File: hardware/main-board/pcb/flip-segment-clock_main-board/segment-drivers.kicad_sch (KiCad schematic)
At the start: 0 parts

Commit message: Refining design of the segment drivers
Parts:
- added C15, C16, C17, C18, C19, C20, C21, C22, C23, C24, C25, C26, C27, C28, C7, C8: 100 nF, Capacitor_SMD:C_0402_1005Metric, symbol Device:C_Small
- added C5: 10 uF, Capacitor_SMD:C_1206_3216Metric, symbol Device:C_Small
- added C6: 560 uF, Capacitor_SMD:C_Elec_10x10.2, symbol Device:C_Polarized_Small
- added D1, D2, D3, D4: D_Schottky_Small, symbol Device:D_Schottky_Small
- added IC10, IC11, IC12, IC13, IC14, IC15, IC16, IC17, IC4, IC5, IC6, IC7, IC8, IC9: A3909GLNTR-T, SamacSys_Parts:SOP100P600X175-10N, symbol SamacSys_Parts:A3909GLNTR-T
- added J3: Digit 1, TerminalBlock:TerminalBlock_Xinya_XY308-2.54-14P_1x14_P2.54mm_Horizontal, symbol Connector:Screw_Terminal_01x14
- added J4: Digit 2, TerminalBlock:TerminalBlock_Xinya_XY308-2.54-14P_1x14_P2.54mm_Horizontal, symbol Connector:Screw_Terminal_01x14
- added J5: Digit 3, TerminalBlock:TerminalBlock_Xinya_XY308-2.54-14P_1x14_P2.54mm_Horizontal, symbol Connector:Screw_Terminal_01x14
- added J6: Digit 4, TerminalBlock:TerminalBlock_Xinya_XY308-2.54-14P_1x14_P2.54mm_Horizontal, symbol Connector:Screw_Terminal_01x14
- added R5, R6: 100K, Resistor_SMD:R_0402_1005Metric, symbol Device:R_Small
- added TP3: SER, TestPoint:TestPoint_Pad_D1.5mm, symbol Connector:TestPoint
- added TP4: 12v, TestPoint:TestPoint_Pad_D1.5mm, symbol Connector:TestPoint
- added U1, U2: 74HC595, Package_SO:SOIC-16_3.9x9.9mm_P1.27mm, symbol 74xx:74HC595
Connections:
- new net: IC11.10 (OUT1), J5.1 (Pin_1)
- new net: IC11.6 (OUT4), J5.4 (Pin_4)
- new net: IC11.7 (OUT3), J5.3 (Pin_3)
- new net: IC11.9 (OUT2), J5.2 (Pin_2)
- new net: C25.2, D3.1 (K), D4.1 (K), IC14.3 (VBB)
- new net: IC16.10 (OUT1), J6.7 (Pin_7)
- new net: IC16.6 (OUT4), J6.10 (Pin_10)
- new net: IC16.7 (OUT3), J6.9 (Pin_9)
- new net: IC16.9 (OUT2), J6.8 (Pin_8)
- new net: IC4.10 (OUT1), J3.1 (Pin_1)
- new net: IC6.9 (OUT2), J3.10 (Pin_10)
- new net: IC6.7 (OUT3), J3.11 (Pin_11)
- new net: IC6.6 (OUT4), J3.12 (Pin_12)
- new net: IC7.10 (OUT1), J3.13 (Pin_13)
- new net: IC7.9 (OUT2), J3.14 (Pin_14)
- new net: IC4.9 (OUT2), J3.2 (Pin_2)
- new net: IC4.7 (OUT3), J3.3 (Pin_3)
- new net: IC4.6 (OUT4), J3.4 (Pin_4)
- new net: IC5.10 (OUT1), J3.5 (Pin_5)
- new net: IC5.9 (OUT2), J3.6 (Pin_6)
- new net: IC5.7 (OUT3), J3.7 (Pin_7)
- new net: IC5.6 (OUT4), J3.8 (Pin_8)
- new net: IC6.10 (OUT1), J3.9 (Pin_9)
- new net: IC13.9 (OUT2), J5.10 (Pin_10)
- new net: IC13.7 (OUT3), J5.11 (Pin_11)
- new net: IC13.6 (OUT4), J5.12 (Pin_12)
- new net: IC14.10 (OUT1), J5.13 (Pin_13)
- new net: IC14.9 (OUT2), J5.14 (Pin_14)
- new net: IC12.10 (OUT1), J5.5 (Pin_5)
- new net: IC12.9 (OUT2), J5.6 (Pin_6)
- new net: IC12.7 (OUT3), J5.7 (Pin_7)
- new net: IC12.6 (OUT4), J5.8 (Pin_8)
- new net: IC13.10 (OUT1), J5.9 (Pin_9)
- new net: U1.9 (QH'), U2.14 (SER)
- new net: C18.2, D1.1 (K), D2.1 (K), IC7.3 (VBB)
- new net: IC9.10 (OUT1), J4.7 (Pin_7)
- new net: IC9.6 (OUT4), J4.10 (Pin_10)
- new net: IC9.7 (OUT3), J4.9 (Pin_9)
- new net: IC9.9 (OUT2), J4.8 (Pin_8)
- new net: IC15.10 (OUT1), J6.3 (Pin_3)
- new net: IC15.6 (OUT4), J6.6 (Pin_6)
- new net: IC15.7 (OUT3), J6.5 (Pin_5)
- new net: IC15.9 (OUT2), J6.4 (Pin_4)
- new net: TP3.1, U1.14 (SER)
- new net: IC14.7 (OUT3), J6.1 (Pin_1)
- new net: IC17.10 (OUT1), J6.11 (Pin_11)
- new net: IC17.9 (OUT2), J6.12 (Pin_12)
- new net: IC17.7 (OUT3), J6.13 (Pin_13)
- new net: IC17.6 (OUT4), J6.14 (Pin_14)
- new net: IC14.6 (OUT4), J6.2 (Pin_2)
- new net: IC7.6 (OUT4), J4.2 (Pin_2)
- new net: IC7.7 (OUT3), J4.1 (Pin_1)
- new net: IC8.10 (OUT1), J4.3 (Pin_3)
- new net: IC8.6 (OUT4), J4.6 (Pin_6)
- new net: IC8.7 (OUT3), J4.5 (Pin_5)
- new net: IC8.9 (OUT2), J4.4 (Pin_4)
- new net: IC10.10 (OUT1), J4.11 (Pin_11)
- new net: IC10.9 (OUT2), J4.12 (Pin_12)
- new net: IC10.7 (OUT3), J4.13 (Pin_13)
- new net: IC10.6 (OUT4), J4.14 (Pin_14)
- new net +12V: C5.2, C6.1, TP4.1
- new net +3.3V: C7.2, C8.2, R5.1, R6.1, U1.16 (VCC), U2.16 (VCC)
- new net A1: U1.15 (QA)
- new net A2: U1.1 (QB)
- new net B3: U1.2 (QC)
- new net B4: U1.3 (QD)
- new net C1: U1.4 (QE)
- new net C2: U1.5 (QF)
- new net C3: U1.6 (QG)
- new net C4: U1.7 (QH)
- new net D1: U2.15 (QA)
- new net D2: U2.1 (QB)
- new net DIG1: C15.2, C16.2, C17.2, D1.2 (A), IC4.3 (VBB), IC5.3 (VBB), IC6.3 (VBB)
- new net DIG2: C19.2, C20.2, C21.2, D2.2 (A), IC10.3 (VBB), IC8.3 (VBB), IC9.3 (VBB)
- new net DIG3: C22.2, C23.2, C24.2, D4.2 (A), IC11.3 (VBB), IC12.3 (VBB), IC13.3 (VBB)
- new net DIG4: C26.2, C27.2, C28.2, D3.2 (A), IC15.3 (VBB), IC16.3 (VBB), IC17.3 (VBB)
- new net E3: U2.2 (QC)
- new net E4: U2.3 (QD)
- new net F1: U2.4 (QE)
- new net F2: U2.5 (QF)
- new net GND: C15.1, C16.1, C17.1, C18.1, C19.1, C20.1, C21.1, C22.1, C23.1, C24.1, C25.1, C26.1, C27.1, C28.1, C5.1, C6.2, C7.1, C8.1, IC10.8 (GND), IC11.8 (GND), IC12.8 (GND), IC13.8 (GND), IC14.8 (GND), IC15.8 (GND), IC16.8 (GND), IC17.8 (GND), IC4.8 (GND), IC5.8 (GND), IC6.8 (GND), IC7.8 (GND), IC8.8 (GND), IC9.8 (GND), U1.8 (GND), U2.8 (GND)
- new net NOE: U1.13 (~{OE}), U2.13 (~{OE})
- new net NSRCLR: R5.2, U1.10 (~{SRCLR}), U2.10 (~{SRCLR})
- new net RCLCK: U1.12 (RCLK), U2.12 (RCLK)
- new net SRCLK: R6.2, U1.11 (SRCLK), U2.11 (SRCLK)
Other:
- note added: "A3909 Cluster"
- note added: "Bypass and Bulk Decoupling"
- note added: "H-Bridge Drivers"
- note added: "One 100 nF cap per IC, one 10 uF and one 470 uF for bulk (prevent major voltage droop during pulses)"
- note added: "Placeholder explaination"

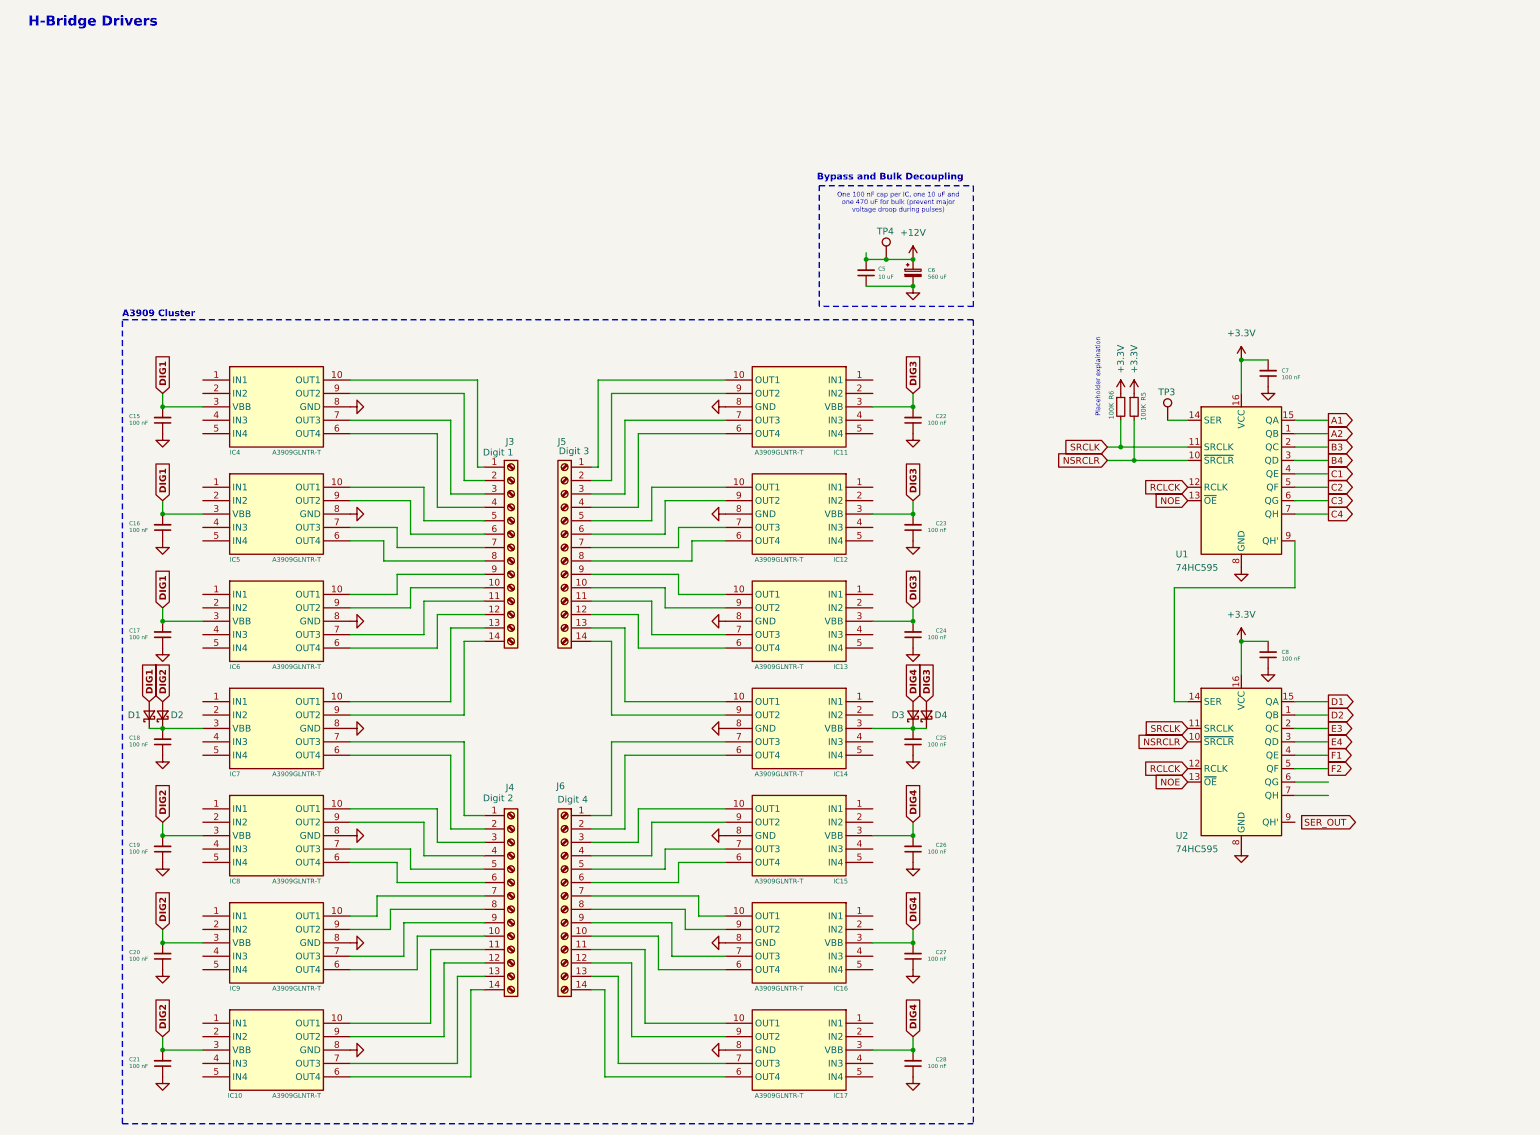
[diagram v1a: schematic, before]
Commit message: Segment driver update
Continuing refinement of segment driver design, settle on per digit vbb isolation, no overlapping between a3909
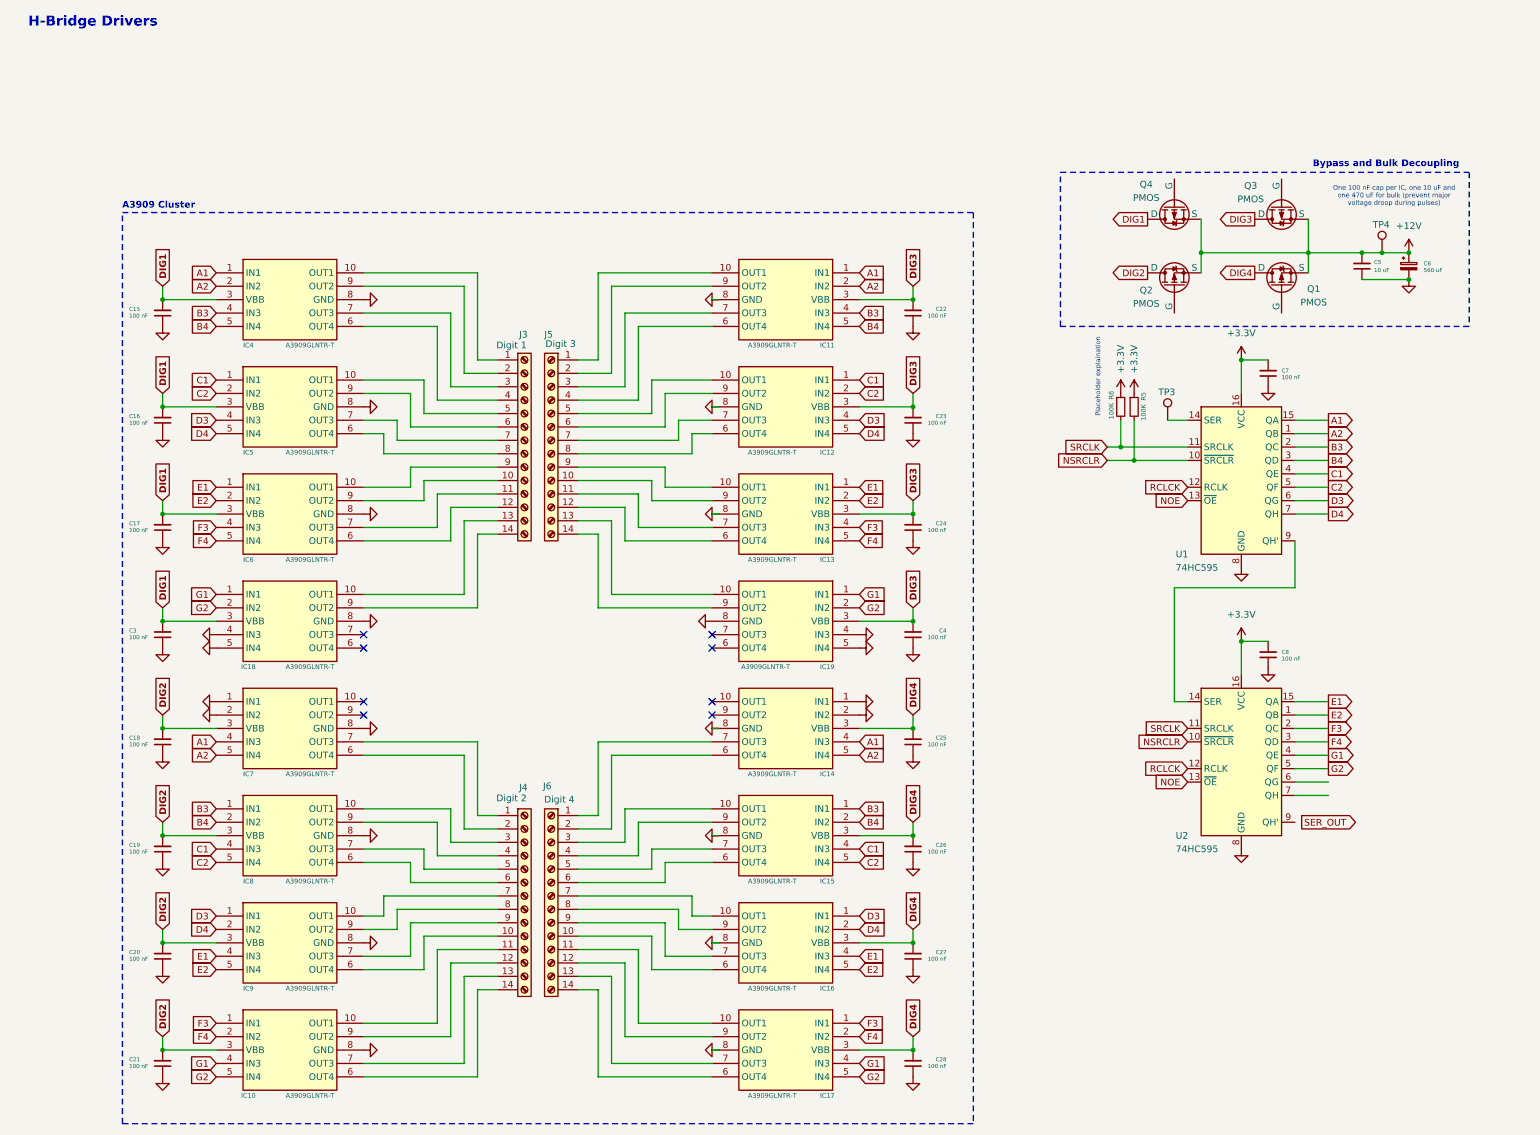
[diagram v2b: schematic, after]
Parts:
- removed D1, D2, D3, D4: D_Schottky_Small, symbol Device:D_Schottky_Small
- added C3, C4: 100 nF, Capacitor_SMD:C_0402_1005Metric, symbol Device:C_Small
- added IC18, IC19: A3909GLNTR-T, SamacSys_Parts:SOP100P600X175-10N, symbol SamacSys_Parts:A3909GLNTR-T
- added Q1, Q2, Q3, Q4: PMOS, symbol Simulation_SPICE:PMOS
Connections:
- net C3 is gone; now on net D3: U1.6 (QG)
- net C4 is gone; now on net D4: U1.7 (QH)
- net D1 is gone; now on net E1: U2.15 (QA)
- net D2 is gone; now on net E2: U2.1 (QB)
- net E3 is gone; now on net F3: U2.2 (QC)
- net E4 is gone; now on net F4: U2.3 (QD)
- net F1 is gone; now on net G1: U2.4 (QE)
- net F2 is gone; now on net G2: U2.5 (QF)
- net +12V: now also Q1.3 (S), Q2.3 (S), Q3.3 (S), Q4.3 (S)
- net A1: now also IC11.1 (IN1), IC14.4 (IN3), IC4.1 (IN1), IC7.4 (IN3)
- net A2: now also IC11.2 (IN2), IC14.5 (IN4), IC4.2 (IN2), IC7.5 (IN4)
- net B3: now also IC11.4 (IN3), IC15.1 (IN1), IC4.4 (IN3), IC8.1 (IN1)
- net B4: now also IC11.5 (IN4), IC15.2 (IN2), IC4.5 (IN4), IC8.2 (IN2)
- net C1: now also IC12.1 (IN1), IC15.4 (IN3), IC5.1 (IN1), IC8.4 (IN3)
- net C2: now also IC12.2 (IN2), IC15.5 (IN4), IC5.2 (IN2), IC8.5 (IN4)
- net DIG1: now also C3.2, IC18.3 (VBB), Q4.1 (D)
- net DIG2: now also C18.2, IC7.3 (VBB), Q2.1 (D)
- net DIG3: now also C4.2, IC19.3 (VBB), Q3.1 (D)
- net DIG4: now also C25.2, IC14.3 (VBB), Q1.1 (D)
- net GND: now also IC14.1 (IN1), IC14.2 (IN2), IC7.1 (IN1), IC7.2 (IN2), C3.1, C4.1, IC18.4 (IN3), IC18.5 (IN4), IC18.8 (GND), IC19.4 (IN3), IC19.5 (IN4), IC19.8 (GND)
- net D3: now reaches IC16.1 (IN1)
- net D3: now also IC12.4 (IN3), IC5.4 (IN3), IC9.1 (IN1)
- net D4: now reaches IC16.2 (IN2)
- net D4: now also IC12.5 (IN4), IC5.5 (IN4), IC9.2 (IN2)
- net E1: now reaches IC16.4 (IN3)
- net E1: now also IC13.1 (IN1), IC6.1 (IN1), IC9.4 (IN3)
- net E2: now reaches IC16.5 (IN4)
- net E2: now also IC13.2 (IN2), IC6.2 (IN2), IC9.5 (IN4)
- net at J3.13 (Pin_13): now also IC18.10 (OUT1); no longer IC7.10 (OUT1)
- net at J3.14 (Pin_14): now also IC18.9 (OUT2); no longer IC7.9 (OUT2)
- net at J5.13 (Pin_13): now also IC19.10 (OUT1); no longer IC14.10 (OUT1)
- net at J5.14 (Pin_14): now also IC19.9 (OUT2); no longer IC14.9 (OUT2)
- net F3: now reaches IC6.4 (IN3)
- net F3: now also IC10.1 (IN1), IC13.4 (IN3), IC17.1 (IN1)
- net F4: now reaches IC6.5 (IN4)
- net F4: now also IC10.2 (IN2), IC13.5 (IN4), IC17.2 (IN2)
- net G1: now reaches IC17.4 (IN3)
- net G1: now also IC10.4 (IN3), IC18.1 (IN1), IC19.1 (IN1)
- net G2: now reaches IC17.5 (IN4)
- net G2: now also IC10.5 (IN4), IC18.2 (IN2), IC19.2 (IN2)
- no-connect marks 0 -> 8
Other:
- moved on the sheet: C15, C16, C17, C22, C23, C24, C5, C6, IC10, IC11, IC12, IC13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

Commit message: Finalizing design of digit VBB isolation
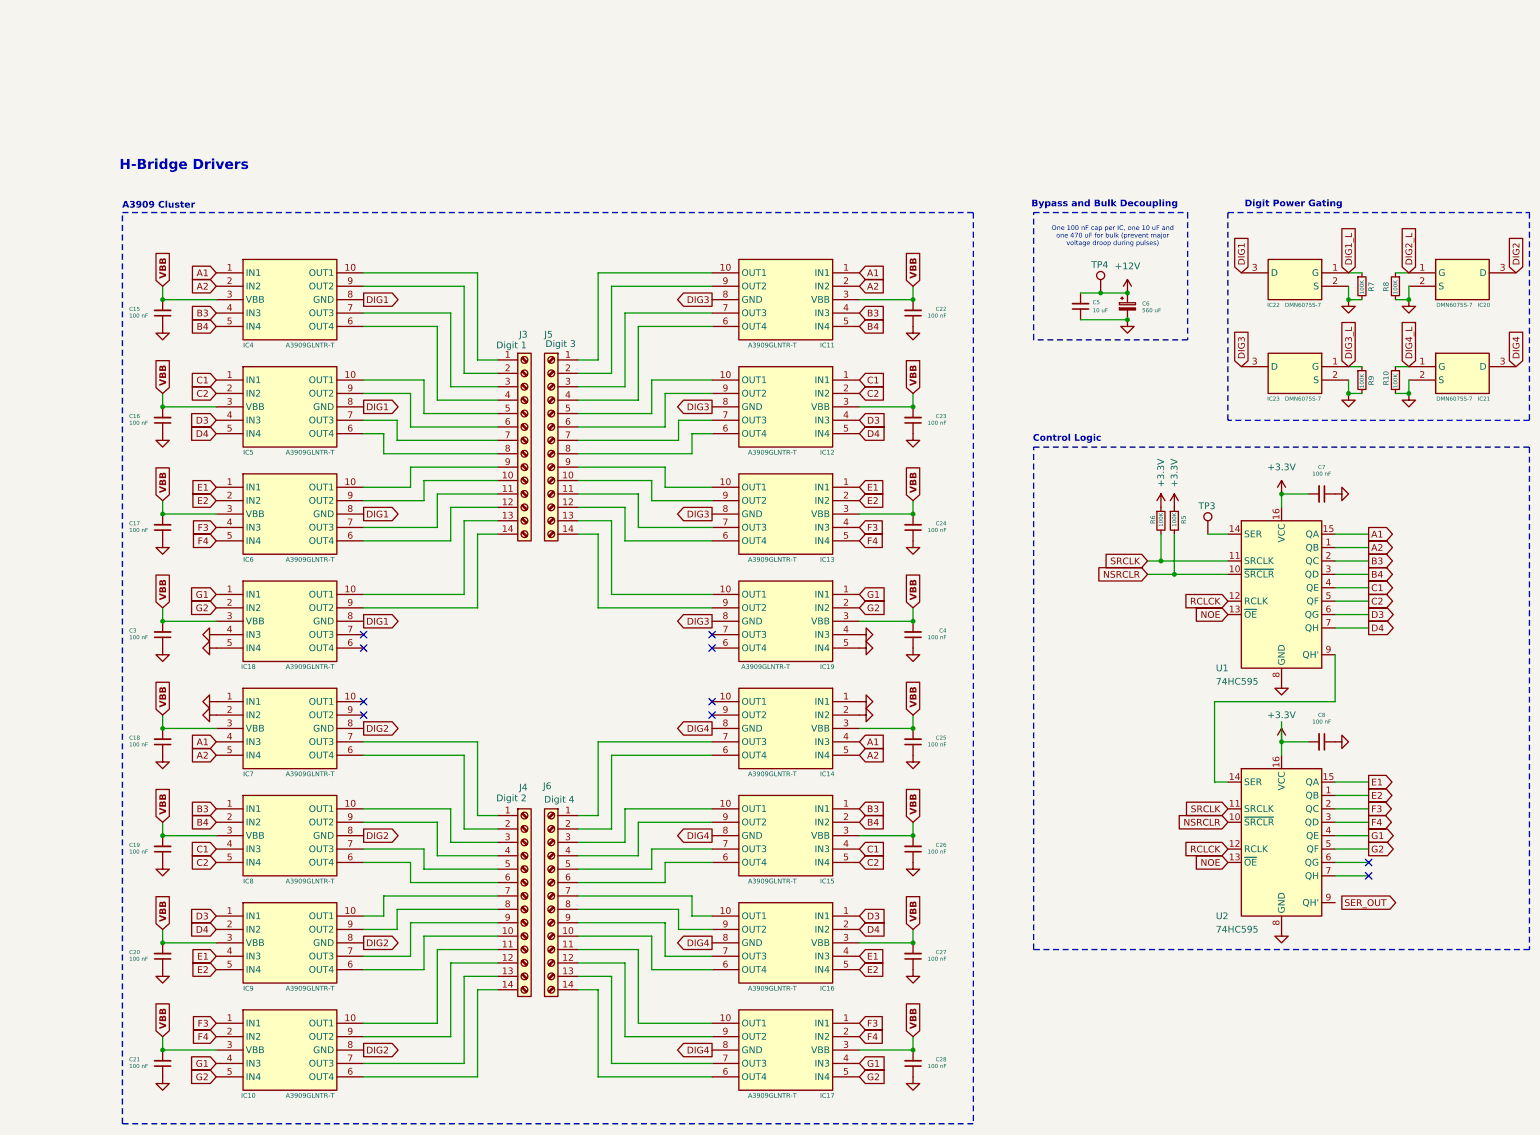
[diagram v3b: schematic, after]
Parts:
- removed Q1, Q2, Q3, Q4: PMOS, symbol Simulation_SPICE:PMOS
- added IC20, IC21, IC22, IC23: DMN6075S-7, SOT96P240X110-3N, symbol SamacSys_Parts:DMN6075S-7
- added R10, R7, R8, R9: 100K, symbol Device:R_Small
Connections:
- net DIG1: now also IC18.8 (GND), IC4.8 (GND), IC5.8 (GND), IC6.8 (GND), IC22.3 (D); no longer C15.2, C16.2, C17.2, C3.2, IC18.3 (VBB), IC4.3 (VBB), IC5.3 (VBB), IC6.3 (VBB)
- net DIG2: now also IC10.8 (GND), IC7.8 (GND), IC8.8 (GND), IC9.8 (GND), IC20.3 (D); no longer C18.2, C19.2, C20.2, C21.2, IC10.3 (VBB), IC7.3 (VBB), IC8.3 (VBB), IC9.3 (VBB)
- net DIG3: now also IC11.8 (GND), IC12.8 (GND), IC13.8 (GND), IC19.8 (GND), IC23.3 (D); no longer C22.2, C23.2, C24.2, C4.2, IC11.3 (VBB), IC12.3 (VBB), IC13.3 (VBB), IC19.3 (VBB)
- net DIG4: now also IC14.8 (GND), IC15.8 (GND), IC16.8 (GND), IC17.8 (GND), IC21.3 (D); no longer C25.2, C26.2, C27.2, C28.2, IC14.3 (VBB), IC15.3 (VBB), IC16.3 (VBB), IC17.3 (VBB)
- net GND: now also IC20.2 (S), IC21.2 (S), IC22.2 (S), IC23.2 (S), R10.2, R7.2, R8.2, R9.2; no longer IC10.8 (GND), IC11.8 (GND), IC12.8 (GND), IC13.8 (GND), IC14.8 (GND), IC15.8 (GND), IC16.8 (GND), IC17.8 (GND), IC18.8 (GND), IC19.8 (GND), IC4.8 (GND), IC5.8 (GND), IC6.8 (GND), IC7.8 (GND), IC8.8 (GND), IC9.8 (GND)
- new net DIG1_L: IC22.1 (G), R7.1
- new net DIG2_L: IC20.1 (G), R8.1
- new net DIG3_L: IC23.1 (G), R9.1
- new net DIG4_L: IC21.1 (G), R10.1
- new net VBB: C15.2, C16.2, C17.2, C18.2, C19.2, C20.2, C21.2, C22.2, C23.2, C24.2, C25.2, C26.2, C27.2, C28.2, C3.2, C4.2, IC10.3 (VBB), IC11.3 (VBB), IC12.3 (VBB), IC13.3 (VBB), IC14.3 (VBB), IC15.3 (VBB), IC16.3 (VBB), IC17.3 (VBB), IC18.3 (VBB), IC19.3 (VBB), IC4.3 (VBB), IC5.3 (VBB), IC6.3 (VBB), IC7.3 (VBB), IC8.3 (VBB), IC9.3 (VBB)
- no-connect marks 8 -> 10
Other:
- note added: "Control Logic"
- note added: "Digit Power Gating"
- note removed: "Placeholder explaination"
- moved on the sheet: C5, C6, C7, C8, R5, R6, TP3, TP4, U1, U2

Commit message: Changelog/design notes for Segment Drivers
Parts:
- IC20, IC21, IC22, IC23: footprint SOT96P240X110-3N -> SamacSys_Parts:SOT96P240X110-3N
- R10, R7, R8, R9: footprint (none) -> Resistor_SMD:R_0402_1005Metric
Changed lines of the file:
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@@
 			)
 		)
-		(property "Footprint" "SOT96P240X110-3N"
+		(property "Footprint" "SamacSys_Parts:SOT96P240X110-3N"
 			(at 229.87 130.48 0)
 			(effects
@@
 			)
 		)
-		(property "Footprint" ""
+		(property "Footprint" "Resistor_SMD:R_0402_1005Metric"
 			(at 248.92 55.88 0)
 			(effects
@@
 			)
 		)
-		(property "Footprint" "SOT96P240X110-3N"
+		(property "Footprint" "SamacSys_Parts:SOT96P240X110-3N"
 			(at 274.32 130.48 0)
 			(effects
@@
 			)
 		)
-		(property "Footprint" "SOT96P240X110-3N"
+		(property "Footprint" "SamacSys_Parts:SOT96P240X110-3N"
 			(at 274.32 148.26 0)
 			(effects
@@
 			)
 		)
-		(property "Footprint" ""
+		(property "Footprint" "Resistor_SMD:R_0402_1005Metric"
 			(at 255.27 38.1 0)
 			(effects
@@
 			)
 		)
-		(property "Footprint" ""
+		(property "Footprint" "Resistor_SMD:R_0402_1005Metric"
 			(at 248.92 38.1 0)
 			(effects
@@
 			)
 		)
-		(property "Footprint" ""
+		(property "Footprint" "Resistor_SMD:R_0402_1005Metric"
 			(at 255.27 55.88 0)
 			(effects
@@
 			)
 		)
-		(property "Footprint" "SOT96P240X110-3N"
+		(property "Footprint" "SamacSys_Parts:SOT96P240X110-3N"
 			(at 229.87 148.26 0)
 			(effects
